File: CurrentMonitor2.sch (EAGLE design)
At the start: 32 parts, among them IC1 MEGA8-AI, IC3 INA168, IC4 MAX3232CWE, J1 AVR_SPI_PRG_6OFFSET_PADS, Q1 10MHz, Q2 BSS123, U1 LCD-16X2NOSILK, X1 AKL701_213, X2 AKL701_213

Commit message: Added RS485 and WiFi options, finalized some parts of the design including order codes and prices @100pcs
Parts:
- removed 0.003: WSL36373L000FEB, R-Vishay:SHUNT-4CSM3675M
- removed IC4: MAX3232CWE, maxim:MAX3232CWE
- removed R7: 20k, rcl:R-TRIMM64W
- added C10, C11, C12, C13, C22: 100n, resistor:C-EUC0805
- added C14, C15: 22p, rcl:C-EUC0805
- added C16: 10µ, rcl:CPOL-EUB
- added C17: 22µ, rcl:CPOL-EUB
- added C19: 220µ, rcl:CPOL-EUD
- added C20, C24, C27, C31: 100n, rcl:C-EUC0805
- added C23: 100µ 63V, rcl:CPOL-EUG
- added C25: 220µ 10V, rcl:CPOL-EUD
- added D2: SK310A, diode:DIODE-DO214AC
- added DC1: VA-0505S, dc-dc-converter:VA-0505S
- added IC12: 75176AD, 751xx:75176AD
- added IC2: NCP1117ST33T3G, burr-brown:REG1117
- added IC5: MCP3426A0-E/SN, MCP3428:MCP3426A0-E/SN
- added JP11, JP12, JP13: (no value), jumper:JP1E
- added L1: 2x51µH, epcos-b82790c0:EPCOS_B82790C0
- added L2: 120µH, inductor-coilcraft:MSS1260
- added OK30, OK31, OK32: ACPL-M50L, ACPL-M50L:ACPL-M50L
- added Q3: 10MHz, crystal:CRYSTALHC49UP
- added R11: 1k, rcl:R-EU_R0805
- added R12: 120, rcl:R-EU_R0805
- added R13, R14: 680, rcl:R-EU_R0805
- added R34, R35, R36: 1k, resistor:R-EU_R0805
- added R73, R74, R75: 220, resistor:R-EU_R0805
- added RS1: WSL36373L000FEB, R-Vishay:SHUNT-4CSM3675M
- added U$2: LM2591HV, LM2591:LM2591HV
- added U$3: (no value), Carambola2:CARAMBOLA2
- added U2: MAX232SOIC16, SparkFun:MAX232SOIC16
- added U3: FT232RL-BASICSSOP, SparkFun:FT232RL-BASICSSOP
- added U4: CD74HC4050M, SparkFun:HEX_CONVERTER
- added U5: SC16IS740IPW,112, MCP3428:SC16IS740IPW,112
- added X4: SD-CONNECTOR104G-TAA0-R, con-sd-attend:SD-CONNECTOR104G-TAA0-R
- added X5: (no value), con-subd:F09HP
- C1, C2: OC_FARNELL (none) -> 1759985; PRICE_100 (none) -> 0.005
- C3, C4, C5, C6: value (none) -> 0.1µ; OC_FARNELL (none) -> 9697039RL; PRICE_100 (none) -> 0.074
- C7, C8: device rcl:C-EUC1206 -> rcl:C-EUC0805; OC_FARNELL (none) -> 1759195RL; PRICE_100 (none) -> 0.005
- IC1: value MEGA8-AI -> ATMEGA168A-AU; OC_FARNELL (none) -> 1841603; PRICE_100 (none) -> 1.32
- IC3: OC_DIGIKEY (none) -> INA168NADKR-ND; OC_FARNELL (none) -> 1206907RL; PRICE_100 (none) -> 1.18
- J1: OC_FARNELL (none) -> 2215302; PRICE_100 (none) -> 0.17
- Q1: OC_FARNELL (none) -> 1842273RL; PRICE_100 (none) -> 0.248
- R1: OC_FARNELL (none) -> 2129195; PRICE_100 (none) -> 0.001
- R10: value 39k -> 33k; OC_FARNELL (none) -> 2129237; PRICE_100 (none) -> 0.001
- R4: value 140k -> 110k; OC_FARNELL (none) -> 2129278; PRICE_100 (none) -> 0.001
- R8: OC_FARNELL (none) -> 2129354; PRICE_100 (none) -> 0.001
- X1, X2: value AKL701_213 -> 1714955; OC_DIGIKEY (none) -> 277-1269-ND; OC_FARNELL (none) -> 3704683; PRICE_100 (none) -> 0.901
- X3: device con-subd:F09HPS -> con-subd:F09HP
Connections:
- net N$10 renamed CONTRAST
- removed net N$15: C6.+, IC4G$1.V+
- removed net N$7: R10.2, R7.E
- removed net RXD: X3-2.F
- removed net TXD: X3-3.F
- new net CS: IC1.PB0(ICP), U4.1A
- new net DMX_IN_A: L1G$1.4
- new net DMX_IN_B: L1G$2.4
- new net GNDI1: C19.-, C20.2, C24.2, C27.2, DC1.-VOUT, IC12.GND, JP13.2, OK30.C, OK31.EMI, OK32.EMI
- new net N$10: D2.C, L2.P$2, U$2.SW
- new net N$101: IC12.B, L1G$2.1, R12.2, R14.2
- new net N$104: OK30.A, R75.1
- new net N$11: C3.-, U2.C1-
- new net N$116: OK31.A, R74.2
- new net N$133: OK32.A, R73.2
- new net N$17: C11.1, U3.3V3OUT
- new net N$21: C14.2, Q3.2, U5.XTAL1
- new net N$22: C15.2, Q3.1, U5.XTAL2
- new net N$27: U4.1Y, X4.1
- new net N$28: U4.2Y, X4.2
- new net N$30: U4.3Y, X4.5
- new net N$53: IC12.A, JP11.1, L1G$1.1, R13.1
- new net N$85: JP12.2, R13.2
- new net N$86: JP13.1, R14.1
- new net N$89: JP11.2, R12.1
- new net REC$1: IC12.R, R75.2
- new net RE_OUT: IC12.!RE, IC12.DE, OK32.COL, R34.1
- new net RTS: R73.1, U5.!RTS
- new net RXD2_RS232: U2.R2IN, X3.2
- new net RXD_RS485: OK30.COL, R36.2, U5.RX
- new net RXD_TTL_2: U$3.43, U2.R2OUT
- new net TXD2_RS232: U2.T2OUT, X3.3
- new net TXD_OUT: IC12.D, OK31.COL, R35.1
- new net TXD_RS485: R74.1, U5.TX
- new net TXD_TTL_2: U$3.44, U2.T2IN
- new net UART_IRQ: IC1.PD2(INT0), R11.1, U5.!IRQ
- new net USB+: U$3.20, U3.USBDP
- new net USB-: U$3.21, U3.USBDM
- new net VCCIO1: C19.+, C20.1, C24.1, C27.1, DC1.+VOUT, IC12.VCC, JP12.1, OK31.BAS, OK32.BAS, R34.2, R35.2
- new net VIN: C23.+, U$2.VIN
- net +3V3: now also C13.2, C17.+, C22.1, IC2.VOUT, R11.2, U$3.50, U$3.51, U4.VCC, U5.!RESET, U5.I2C, U5.VDD, X4.4
- net +5V: now also C10.1, C12.2, C16.+, C25.+, C31.1, C6.-, DC1.+VIN, IC2.VIN, IC5.VDD, L2.P$1, OK30.BAS, R36.1, U$2.FB, U2.VCC, U3.VCC, U3.VCCIO; no longer IC4P.VCC
- net ADC0: now also IC5.CH1+; no longer IC1.PC0(ADC0)
- net ADC1: now also IC5.CH2+, R10.2, R8.1; no longer IC1.PC1(ADC1), R7.S
- net GND: now also C10.2, C11.2, C12.1, C13.1, C14.1, C15.1, C16.-, C17.-, C22.2, C31.2, DC1.-VIN, IC2.GND, IC5.CH1-, IC5.CH2-, IC5.VSS, OK30.EMI, OK31.C, OK32.C, U$3.22, U$3.25, U$3.27, U$3.28, U$3.29, U$3.30, U$3.31, U$3.32, U$3.34, U$3.42, U$3.45, U$3.46, U$3.47, U$3.48, U$3.49, U$3.7, U2.GND, U3.AGND, U3.GND1, U3.GND2, U3.GND3, U4.GND, U5.A0, U5.A1, U5.VSS, X3.7, X3.G1, X3.G2, X4.3, X4.6, X4.GND1, X4.GND2, X4.GND3, X5.7, X5.G1, X5.G2; no longer C6.-, IC4P.GND, X3-7.F
- net MISO: now also X4.7
- net MOSI: now also U4.2A
- net N$1: now also RS1.S2; no longer 0.003.S2
- net N$12: now also C4.-, U2.C2-; no longer C4.+, IC4G$1.C2+
- net N$13: now also C4.+, U2.C2+; no longer C4.-, IC4G$1.C2-
- net N$14: now also C3.+, U2.C1+; no longer C5.-, IC4G$1.V-
- net N$2: now also RS1.S1; no longer 0.003.S1
- net N$5: now also RS1.I1; no longer 0.003.I1
- net N$6: now also C6.+, U2.V+; no longer C3.-, IC4G$1.C1-
- net N$8: now also C23.-, C25.-, D2.A, U$2.GND; no longer R7.A, R8.1
- net N$9: now also C5.-, U2.V-; no longer C3.+, IC4G$1.C1+
- net RXD_RS232: now also U2.R1IN, X5.2; no longer IC4G$1.R1IN
- net RXD_TTL: now also U2.R1OUT, U3.TXD; no longer IC4G$1.R1OUT
- net SCK: now also U4.3A
- net SCL: now also IC5.SCL, U5.SCL
- net SDA: now also IC5.SDA, U5.SDA
- net TXD_RS232: now also U2.T1OUT, X5.3; no longer IC4G$1.T1OUT
- net TXD_TTL: now also U2.T1IN, U3.RXD; no longer IC4G$1.T1IN
- net VIN_MEAS: now also RS1.I2; no longer 0.003.I2
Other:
- note added: "+3v3"
- note added: "90mV full scale input for INA168"
- note added: "DMX Input"
- note added: "Gain for full-scale ADC input = 22"
- note added: "ISP Connector"
- note added: "Main MCU"
- note added: "Measurement Input"
- note added: "RS232 Level Shifter"
- note added: "RS232 MCU"
- note added: "SD Card Interface"
- note added: "Voltage Divider=3"
- note added: "We're level shifting the signals down to 3V3 so that we're within specs. Library Symbol and Idea from SparkFun."
- note removed: "90mV full scale input"
- note removed: "Dividor=25.641"
- note removed: "Gain for full-scale ADC input =28"
- moved on the sheet: C1, C2, C3, C4, C5, C6, C7, C8, C9, D1, IC1, IC3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

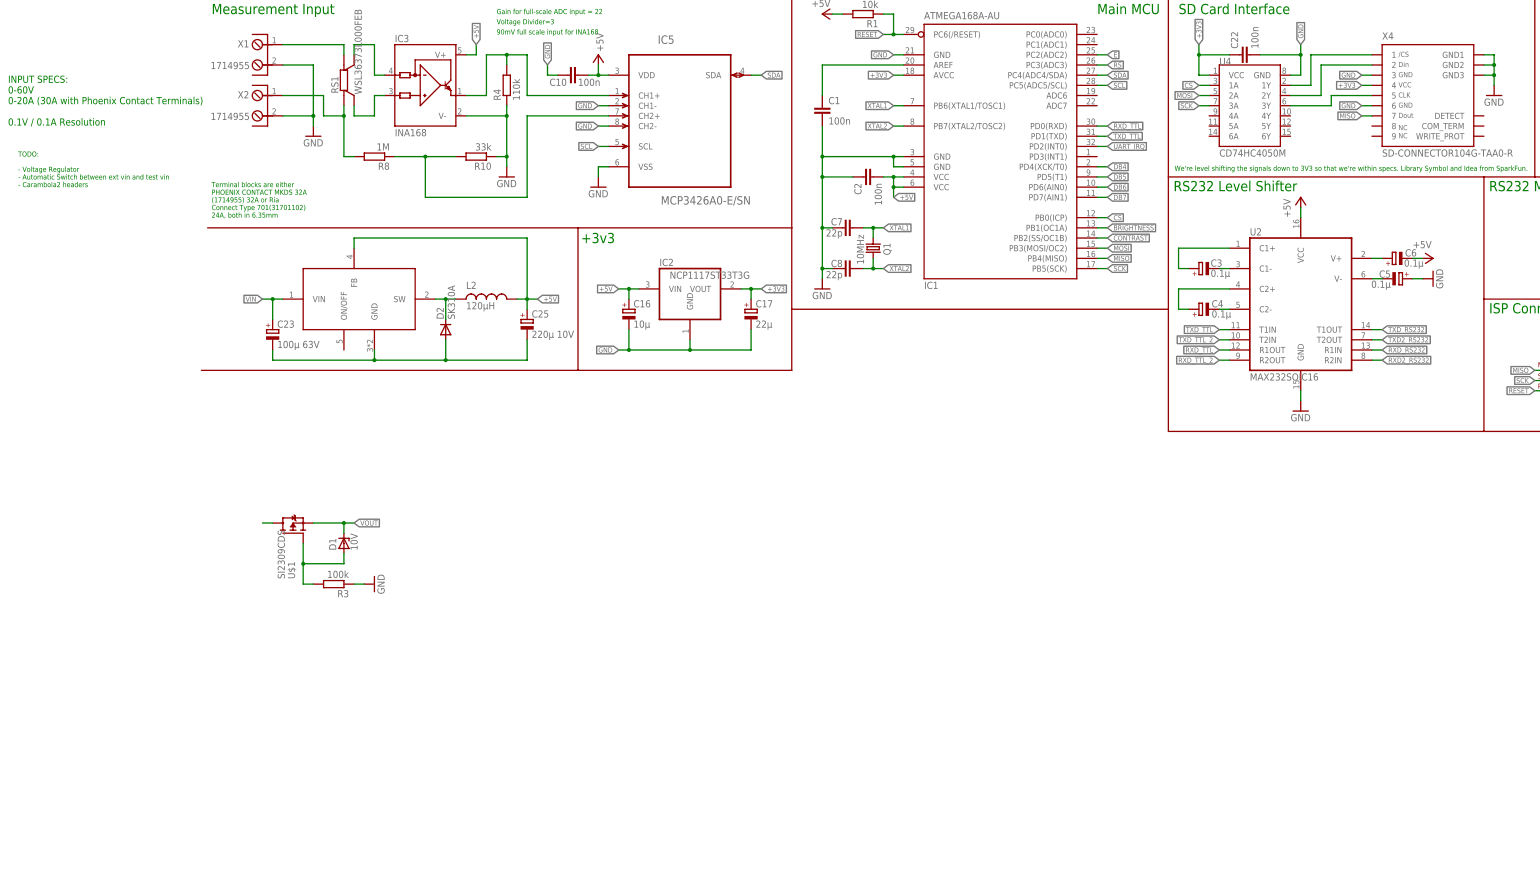
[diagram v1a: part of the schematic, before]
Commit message: Added dual input switching power supplies and power switching circuitry
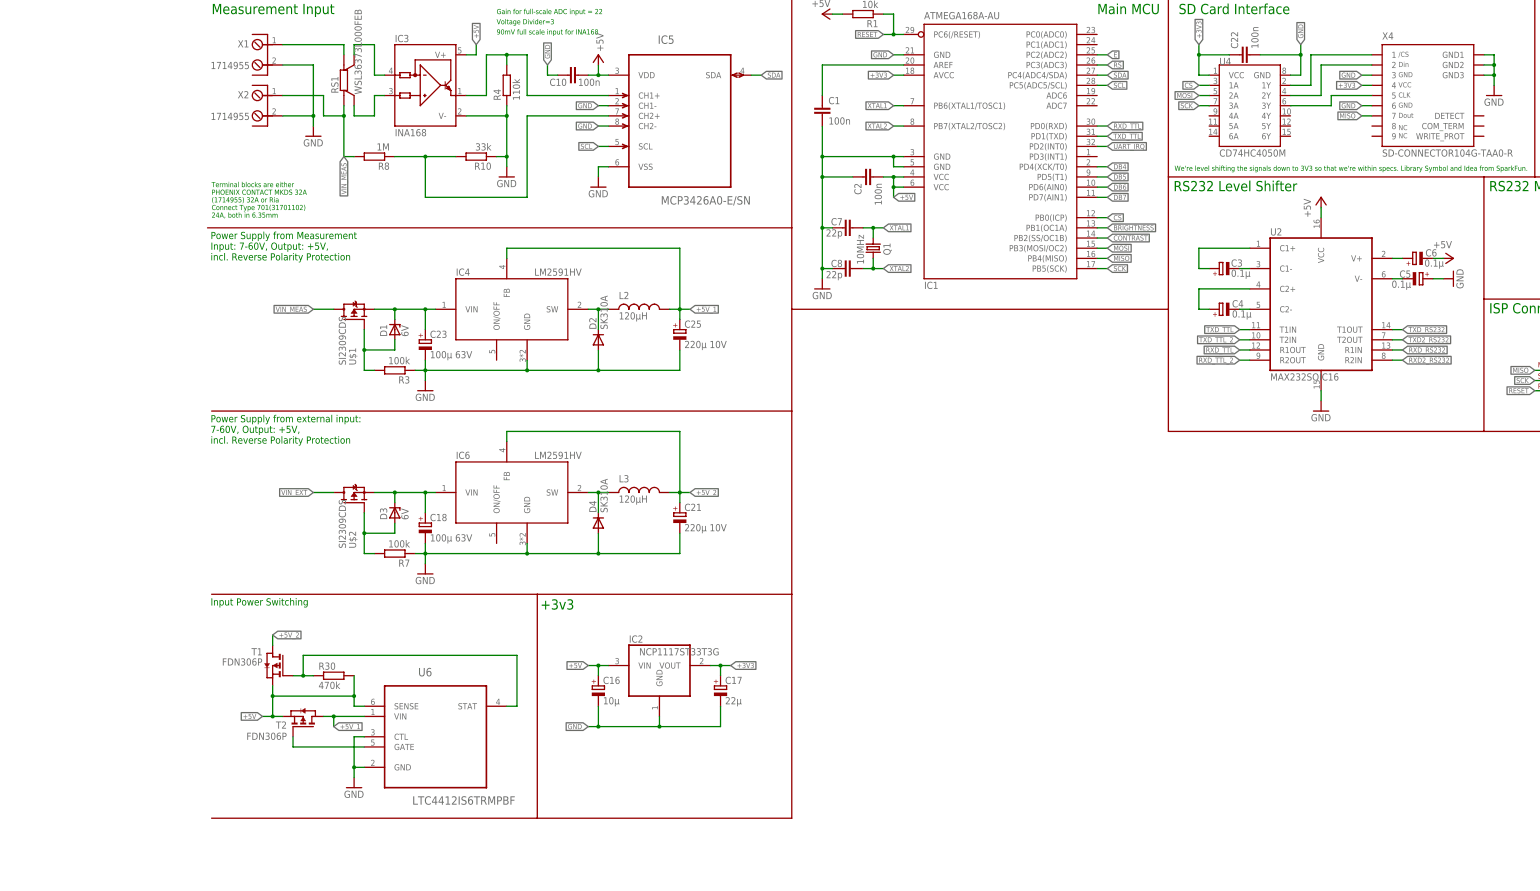
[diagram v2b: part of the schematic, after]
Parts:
- added C18: 100µ 63V, rcl:CPOL-EUG
- added C21: 220µ 10V, rcl:CPOL-EUD
- added D3: 6V, diode:ZENER-DIODESOT23
- added D4: SK310A, diode:DIODE-DO214AC
- added IC4, IC6: LM2591HV, LM2591:LM2591HV
- added L3: 120µH, inductor-coilcraft:MSS1260
- added R30: 470k, rcl:R-EU_R0805
- added R7: 100k, rcl:R-EU_R0805
- added T1, T2: FDN306P, zetex:PMOSSOT23
- added U6: LTC4412IS6TRMPBF, LTC4412:LTC4412IS6TRMPBF
- D1: value 10V -> 6V
- U$2: value LM2591HV -> SI2309CDS; device LM2591:LM2591HV -> Si2309CDS:SI2309CDS; OC_DIGIKEY LM2591HVSX-5.0/NOPBCT-ND -> (none); PRICE_100 2.0529 -> (none)
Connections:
- removed net VOUT: D1.C, U$1.S
- new net +5V_1: C25.+, IC4.FB, L2.P$1, T2.D, U6.VIN
- new net +5V_2: C21.+, IC6.FB, L3.P$1, T1.D
- new net N$15: T2.G, U6.GATE
- new net N$7: D4.C, IC6.SW, L3.P$2
- new net VIN1: C18.+, D3.C, IC6.VIN, U$2.S
- new net VIN_EXT: U$2.D
- net +5V: now also R30.2, T1.S, T2.S, U6.SENSE; no longer C25.+, L2.P$1, U$2.FB
- net GND: now also C18.-, C21.-, C23.-, C25.-, D2.A, D4.A, IC4.GND, IC6.GND, R7.1, U6.CTL, U6.GND
- net N$10: now also IC4.SW; no longer U$2.SW
- net N$3: now also D3.A, R7.2, U$2.G; no longer U$1.D
- net N$8: now also R30.1, T1.G, U6.STAT; no longer C23.-, C25.-, D2.A, U$2.GND
- net VIN: now also D1.C, IC4.VIN, U$1.S; no longer U$2.VIN
- net VIN_MEAS: now also U$1.D
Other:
- note added: "Input Power Switching"
- note added: "Power Supply from Measurement Input: 7-60V, Output: +5V, incl. Reverse Polarity Protection"
- note added: "Power Supply from external input: 7-60V, Output: +5V, incl. Reverse Polarity Protection"
- note removed: "INPUT SPECS: 0-60V 0-20A (30A with Phoenix Contact Terminals) 0.1V / 0.1A Resolution"
- note removed: "TODO: - Voltage Regulator - Automatic Switch between ext vin and test vin - Carambola2 headers"
- moved on the sheet: C16, C17, C23, C25, C3, C4, C5, C6, D1, D2, IC2, L2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
